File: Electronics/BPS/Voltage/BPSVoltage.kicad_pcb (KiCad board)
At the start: 2 copper layers, 69.9 x 59.7 mm, 72 parts, among them J1 Conn1, J2 Conn2, J3 Conn_01x06, J4 Conn_01x07, Q1 BSS308PE, Q10 BSS308PE, Q11 BSS308PE, Q12 BSS308PE, Q13 BSS308PE, Q2 BSS308PE, Q3 BSS308PE, Q4 BSS308PE, Q5 NSV1C201MZ4, Q6 BSS308PE, Q7 BSS308PE, Q8 BSS308PE, Q9 BSS308PE, U1 LTC6811-1, U2 HX1188FNL

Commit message: Got bored and restructured somewhat.
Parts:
- moved R3 29.4 mm to (176.4, 25.9), turned to 0 degrees
- moved R17 21.8 mm to (211.3, 41.2), turned to 270 degrees
- moved R1 21.8 mm to (181.9, 25.9), turned to 180 degrees
- moved R16 21.0 mm to (209.3, 41.2), turned to 270 degrees
- moved C1 19.7 mm to (188.0, 25.9), turned to 0 degrees
- moved C14 18.5 mm to (199.1, 70.0), turned to 270 degrees
- moved C17 18.4 mm to (195.2, 73.7)
- moved U2 16.6 mm to (206.2, 69.1)
- moved Q5 15.4 mm to (205.7, 31.6)
- moved R23 15.0 mm to (214.8, 49.8), turned to 0 degrees
- moved C18 14.1 mm to (217.7, 58.3)
- moved C10 14.1 mm to (211.3, 35.6), turned to 270 degrees
- moved C15 12.7 mm to (215.9, 44.1), turned to 90 degrees
- moved R24 11.4 mm to (215.8, 60.5)
- moved J1 10.2 mm to (222.9, 52.1)
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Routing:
- net Net-(C3-Pad1): track 7.51 -> 35.0 mm
- net /Batt12: track 49.1 -> 22.7 mm
- net GND: track 29.9 -> 14.6 mm
- net Net-(Q5-Pad1): track 6.05 -> 20.0 mm, vias 0 -> 2
- net Net-(R16-Pad1): track 21.4 -> 7.79 mm
- net Net-(J1-Pad1): track 8.34 -> 21.8 mm
- net /VREG: track 13.1 -> 25.4 mm, vias 0 -> 2
- net Net-(R16-Pad2): track 17.0 -> 5.41 mm
- net Net-(J1-Pad2): track 8.15 -> 19.6 mm
- net /IMA: track 35.5 -> 26.0 mm
- net Net-(Q11-Pad1): track 14.1 -> 22.5 mm, vias 2 -> 0
- net Net-(Q12-Pad1): track 21.6 -> 28.8 mm, vias 2 -> 0
- net Net-(C1-Pad1): track 23.7 -> 30.7 mm
- net Net-(J2-Pad1): track 8.36 -> 15.1 mm
- net Net-(J2-Pad2): track 8.55 -> 14.9 mm
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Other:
- board size 69.9 x 59.7 mm -> 58.4 x 59.7 mm
- board text added: "Chase Block"
- board text added: "UT SVT -- BeVolt"
- board text added: "Voltage Slave 2019"
- board text removed: "2019"
- board text removed: "UT Solar Vehicle Team -- BeVolt"
- board text removed: "Voltage Slave Board Designed by Chase Block"

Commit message: Finished up revision 2 of the board.
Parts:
- added D1: LED, LED_SMD:LED_0805_2012Metric, F.Cu at (134.6, 157.0)
- added D10: LED, LED_SMD:LED_0805_2012Metric, F.Cu at (100.8, 124.2)
- added D11: LED, LED_SMD:LED_0805_2012Metric, F.Cu at (97.8, 124.2)
- added D12: LED, LED_SMD:LED_0805_2012Metric, F.Cu at (94.8, 124.2)
- added D13: LED, LED_SMD:LED_0805_2012Metric, F.Cu at (91.9, 124.2)
- added D2: LED, LED_SMD:LED_0805_2012Metric, F.Cu at (129.8, 124.2)
- added D3: LED, LED_SMD:LED_0805_2012Metric, F.Cu at (126.8, 124.2)
- added D4: LED, LED_SMD:LED_0805_2012Metric, F.Cu at (123.8, 124.2)
- added D5: LED, LED_SMD:LED_0805_2012Metric, F.Cu at (120.8, 124.2)
- added D6: LED, LED_SMD:LED_0805_2012Metric, F.Cu at (117.8, 124.2)
- added D7: LED, LED_SMD:LED_0805_2012Metric, F.Cu at (109.8, 124.2)
- added D8: LED, LED_SMD:LED_0805_2012Metric, F.Cu at (106.8, 124.2)
- added D9: LED, LED_SMD:LED_0805_2012Metric, F.Cu at (103.8, 124.2)
- added J5: Conn_01x03, Connector_PinHeader_2.54mm:PinHeader_1x03_P2.54mm_Vertical, F.Cu at (108.9, 181.5)
- added J6: Conn_01x05, Connector_PinHeader_2.54mm:PinHeader_1x05_P2.54mm_Vertical, F.Cu at (98.9, 181.5)
- added J7: Conn_02x03_Counter_Clockwise, Connector_PinHeader_2.54mm:PinHeader_2x03_P2.54mm_Vertical, F.Cu at (82.5, 168.8)
- added L1: Ferrite_Bead, Inductor_SMD:L_0805_2012Metric, F.Cu at (132.8, 119.3)
- added L10: Ferrite_Bead, Inductor_SMD:L_0805_2012Metric, F.Cu at (100.8, 119.3)
- added L11: Ferrite_Bead, Inductor_SMD:L_0805_2012Metric, F.Cu at (97.8, 119.3)
- added L12: Ferrite_Bead, Inductor_SMD:L_0805_2012Metric, F.Cu at (94.8, 119.3)
- added L13: Ferrite_Bead, Inductor_SMD:L_0805_2012Metric, F.Cu at (91.8, 119.3)
- added L14: Ferrite_Bead, Inductor_SMD:L_0805_2012Metric, F.Cu at (87.3, 119.3)
- added L2: Ferrite_Bead, Inductor_SMD:L_0805_2012Metric, F.Cu at (129.8, 119.3)
- added L3: Ferrite_Bead, Inductor_SMD:L_0805_2012Metric, F.Cu at (126.8, 119.3)
- added L4: Ferrite_Bead, Inductor_SMD:L_0805_2012Metric, F.Cu at (123.8, 119.3)
- added L5: Ferrite_Bead, Inductor_SMD:L_0805_2012Metric, F.Cu at (120.8, 119.3)
- added L6: Ferrite_Bead, Inductor_SMD:L_0805_2012Metric, F.Cu at (117.8, 119.3)
- added L7: Ferrite_Bead, Inductor_SMD:L_0805_2012Metric, F.Cu at (109.8, 119.3)
- added L8: Ferrite_Bead, Inductor_SMD:L_0805_2012Metric, F.Cu at (106.8, 119.3)
- added L9: Ferrite_Bead, Inductor_SMD:L_0805_2012Metric, F.Cu at (103.8, 119.3)
- added MH1: MountingHole, MountingHole:MountingHole_3mm, F.Cu at (141.8, 181.8)
- added MH2: MountingHole, MountingHole:MountingHole_3mm, F.Cu at (141.8, 113.2)
- added MH3: MountingHole, MountingHole:MountingHole_3mm, F.Cu at (83.2, 113.2)
- added MH4: MountingHole, MountingHole:MountingHole_3mm, F.Cu at (83.2, 181.8)
- added R33: 1.5k, Resistor_SMD:R_0805_2012Metric, F.Cu at (134.6, 160.9)
- added R34: 1.2k, Resistor_SMD:R_0805_2012Metric, F.Cu at (129.8, 128.1)
- added R35: 1.2k, Resistor_SMD:R_0805_2012Metric, F.Cu at (126.8, 128.1)
- added R36: 1.2k, Resistor_SMD:R_0805_2012Metric, F.Cu at (123.8, 128.1)
- added R37: 1.2k, Resistor_SMD:R_0805_2012Metric, F.Cu at (120.8, 128.1)
- added R38: 1.2k, Resistor_SMD:R_0805_2012Metric, F.Cu at (117.8, 128.1)
- added R39: 1.2k, Resistor_SMD:R_0805_2012Metric, F.Cu at (109.8, 128.1)
- added R40: 1.2k, Resistor_SMD:R_0805_2012Metric, F.Cu at (106.8, 128.1)
- added R41: 1.2k, Resistor_SMD:R_0805_2012Metric, F.Cu at (103.8, 128.1)
- added R42: 1.2k, Resistor_SMD:R_0805_2012Metric, F.Cu at (100.8, 128.1)
- added R43: 1.2k, Resistor_SMD:R_0805_2012Metric, F.Cu at (97.8, 128.1)
- added R44: 1.2k, Resistor_SMD:R_0805_2012Metric, F.Cu at (94.8, 128.1)
- added R45: 1.2k, Resistor_SMD:R_0805_2012Metric, F.Cu at (91.9, 128.1)
- added TP1: V+, TestPoint:TestPoint_Keystone_5005-5009_Compact, F.Cu at (142.2, 119.3)
- added TP2: VREG, TestPoint:TestPoint_Keystone_5005-5009_Compact, F.Cu at (142.2, 136.6)
- added TP3: GND, TestPoint:TestPoint_Keystone_5005-5009_Compact, F.Cu at (142.2, 129.1)
- R16: value 1k -> 806
- R17: value 1k -> 1.21k
- moved J1 176.3 mm to (84.1, 160.9), turned to 90 degrees
- moved C15 163.6 mm to (102.4, 162.0), turned to 0 degrees
- moved R20 163.1 mm to (97.6, 161.1), turned to 270 degrees
- moved J2 161.9 mm to (84.1, 148.3), turned to 90 degrees
- moved R23 156.4 mm to (102.4, 158.6), turned to 180 degrees
- moved R16 154.5 mm to (118.3, 166.0), turned to 90 degrees
- moved R17 154.5 mm to (120.3, 166.0), turned to 90 degrees
- moved C18 154.4 mm to (85.6, 138.3), turned to 90 degrees
- moved C9 152.9 mm to (113.9, 166.6), turned to 270 degrees
- moved C8 152.7 mm to (111.8, 166.6), turned to 270 degrees
- moved C10 152.6 mm to (130.3, 164.9)
- moved C1 151.4 mm to (128.0, 164.9), turned to 270 degrees
- moved Q5 148.9 mm to (128.0, 158.6)
- moved R24 148.9 mm to (92.7, 144.3)
- moved R27 144.5 mm to (96.7, 144.3), turned to 180 degrees
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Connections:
- net Net-(Q1-Pad3) renamed /L11
- net Net-(Q10-Pad3) renamed /L3
- net Net-(Q11-Pad3) renamed /L2
- net Net-(Q12-Pad3) renamed /L1
- net Net-(Q13-Pad3) renamed /L0
- net Net-(Q2-Pad3) renamed /L10
- net Net-(Q3-Pad3) renamed /L9
- net Net-(Q4-Pad3) renamed /L8
- net Net-(Q6-Pad3) renamed /L7
- net Net-(Q7-Pad3) renamed /L6
- net Net-(Q8-Pad3) renamed /L5
- net Net-(Q9-Pad3) renamed /L4
- C21 pad 1: GND -> /Batt0
- J3 pad 1: /Batt7 -> Net-(J3-Pad1)
- J3 pad 2: /Batt8 -> Net-(J3-Pad2)
- J3 pad 3: /Batt9 -> Net-(J3-Pad3)
- J3 pad 4: /Batt10 -> Net-(J3-Pad4)
- J3 pad 5: /Batt11 -> Net-(J3-Pad5)
- J3 pad 6: /Batt12 -> /V12
- J4 pad 1: GND -> Net-(J4-Pad1)
- J4 pad 2: /Batt1 -> Net-(J4-Pad2)
- J4 pad 3: /Batt2 -> Net-(J4-Pad3)
- J4 pad 4: /Batt3 -> Net-(J4-Pad4)
- J4 pad 5: /Batt4 -> Net-(J4-Pad5)
- J4 pad 6: /Batt5 -> Net-(J4-Pad6)
- J4 pad 7: /Batt6 -> Net-(J4-Pad7)
- R1 pad 2: /Batt12 -> /V12
- R3 pad 1: /Batt12 -> /V12
- R32 pad 1: GND -> /Batt0
- U1 pad 26: GND -> /Batt0
- U1 pad 27: (no net) -> /GPIO1
- U1 pad 28: (no net) -> /GPIO2
- U1 pad 29: (no net) -> /GPIO3
- U1 pad 32: (no net) -> /GPIO4
- U1 pad 33: (no net) -> /GPIO5
- U1 pad 40: /VREG -> /ISOMD
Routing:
- net /Batt0: track 0.00 -> 57.9 mm, vias 0 -> 4
- net /VREG: track 25.4 -> 75.1 mm, vias 2 -> 0
- net /IMA: track 26.0 -> 63.2 mm
- net /IPB: track 36.6 -> 66.7 mm, vias 0 -> 2
- net /GPIO1: track 0.00 -> 27.8 mm
- net /GPIO2: track 0.00 -> 26.0 mm
- net /IMB: track 39.6 -> 65.4 mm
- net /GPIO3: track 0.00 -> 25.2 mm
- net /GPIO4: track 0.00 -> 25.0 mm
- net /GPIO5: track 0.00 -> 24.2 mm
- net /ISOMD: track 0.00 -> 23.0 mm, vias 0 -> 2
- net Net-(C3-Pad1): track 35.0 -> 57.8 mm
- net /IPA: track 23.6 -> 46.1 mm, vias 0 -> 3
- net Net-(C16-Pad1): track 35.3 -> 15.4 mm
- net Net-(C1-Pad1): track 30.7 -> 49.6 mm
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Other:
- board size 58.4 x 59.7 mm -> 65 x 75 mm
- board text added: "GND"
- board text added: "V+"
- board text added: "VREG"
- board text removed: "Chase Block"
- board text removed: "UT SVT -- BeVolt"
- board text removed: "Voltage Slave 2019"

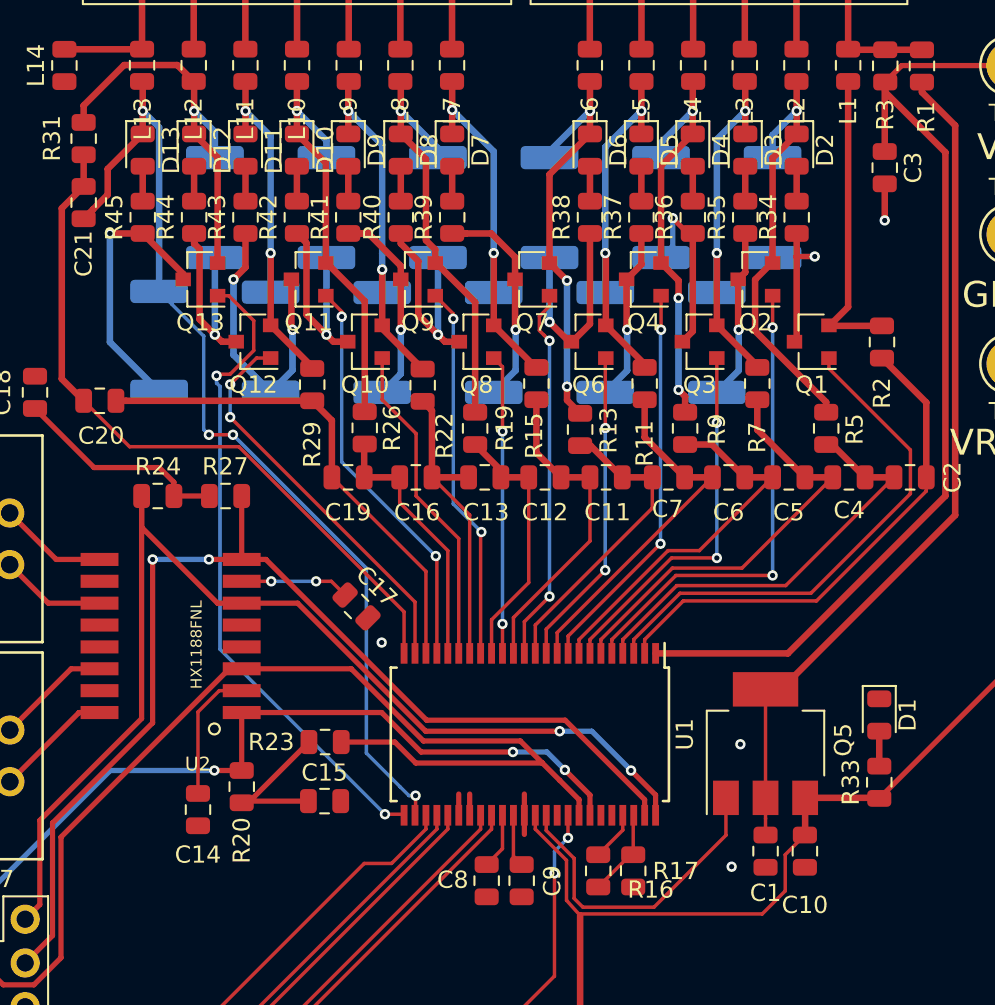
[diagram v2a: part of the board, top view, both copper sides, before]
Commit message: Fixed the via sizes on the voltage board.
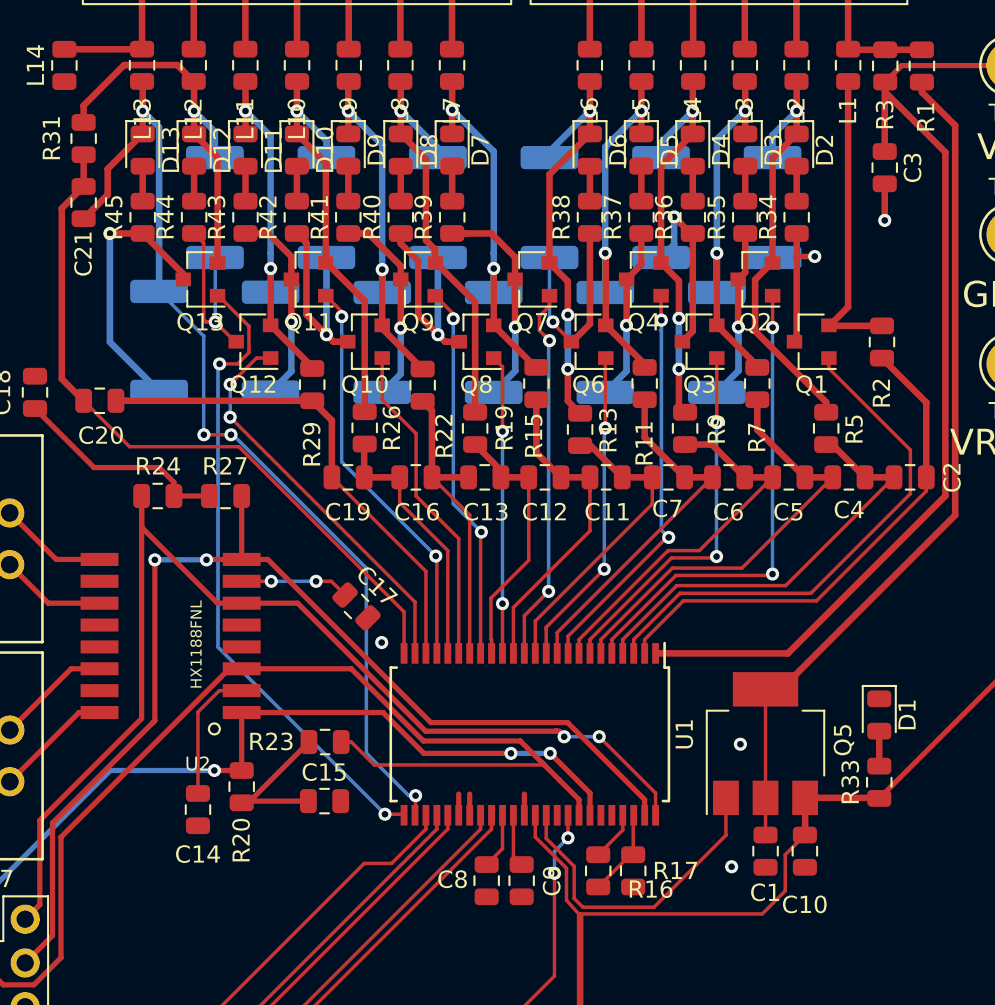
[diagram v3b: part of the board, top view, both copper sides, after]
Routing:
- net /L2: track 17.5 -> 11.6 mm, vias 2 -> 1
- net GND: track 6.94 -> 5.82 mm
- net /Batt6: track 22.3 -> 21.4 mm
- net /Batt2: track 21.9 -> 21.0 mm
- net /L1: track 12.3 -> 11.4 mm
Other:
- net class Default: via_dia 0.8 -> 0.762; via_drill 0.4 -> 0.381
- rule via_min_drill: 0.3 -> 0.381
- rule via_min_size: 0.4 -> 0.762

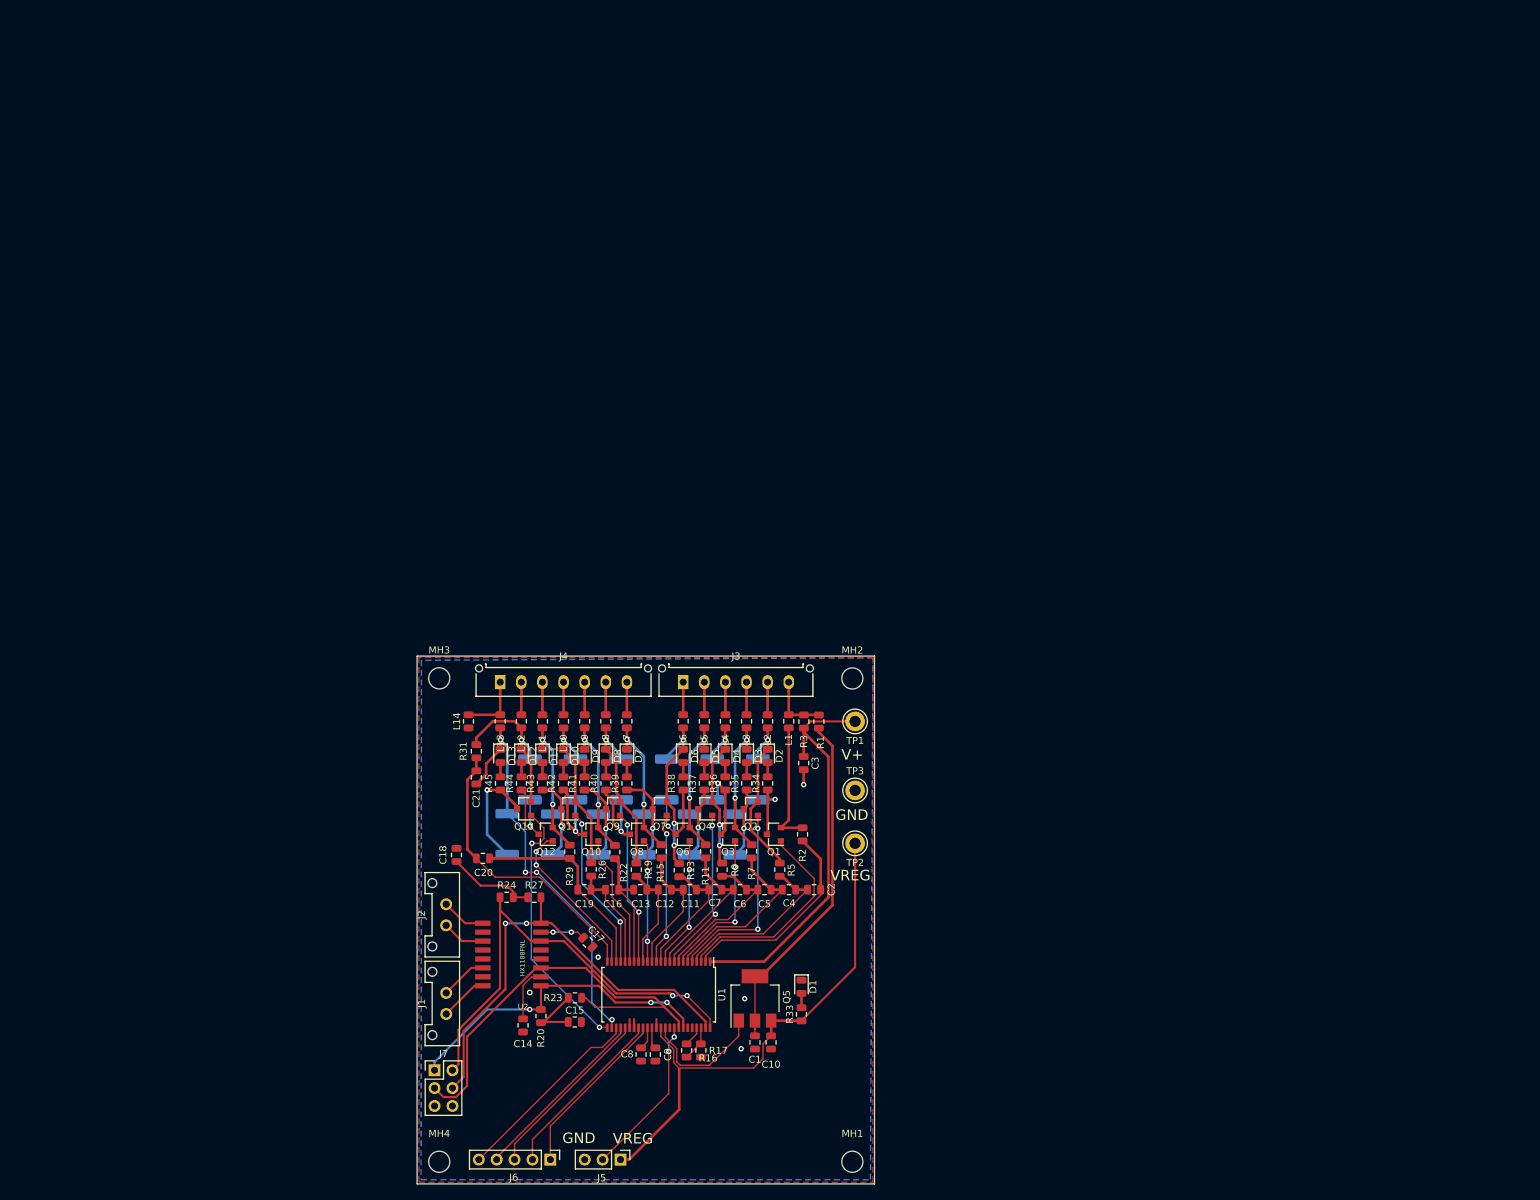
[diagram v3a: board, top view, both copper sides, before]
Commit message: Moved some components around and deleted dimension
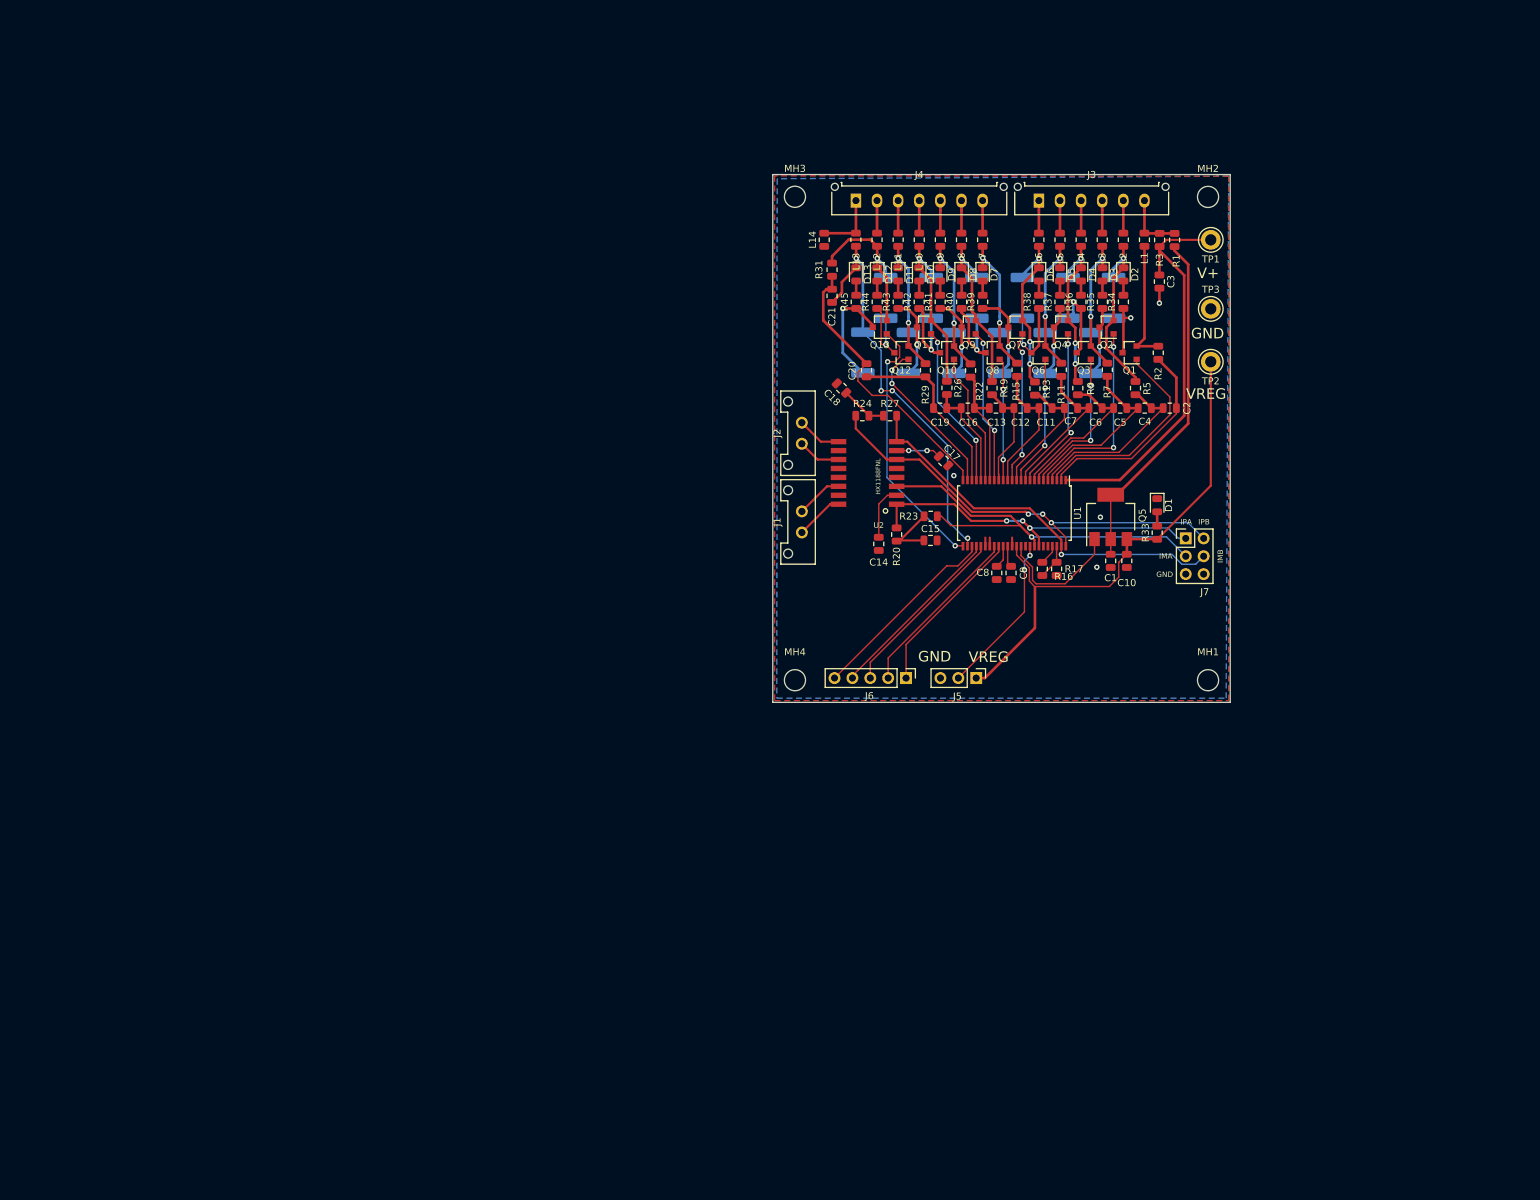
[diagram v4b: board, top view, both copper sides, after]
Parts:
- moved J7 130.8 mm to (189.2, 93.3)
- moved C20 88.2 mm to (143.9, 69.4), turned to 270 degrees
- moved C18 86.0 mm to (140.3, 71.9), turned to 135 degrees
- moved D2 85.1 mm to (180.4, 55.8)
- moved D6 85.1 mm to (168.4, 55.8)
- moved R1 85.1 mm to (187.6, 50.9)
- moved R34 85.1 mm to (180.4, 59.7)
- moved R38 85.1 mm to (168.4, 59.7)
- moved C1 85.1 mm to (178.6, 96.5)
- moved C10 85.1 mm to (180.8, 96.5)
- moved C11 85.1 mm to (169.3, 74.8)
- moved C12 85.1 mm to (165.7, 74.8)
- moved C14 85.1 mm to (145.6, 94.1)
- moved C16 85.1 mm to (158.3, 74.8)
- moved C21 85.1 mm to (139.0, 58.8)
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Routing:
- net /IMB: track 65.3 -> 56.2 mm, vias 2 -> 1
- net Net-(C18-Pad1): track 12.7 -> 6.68 mm
- net /IPB: track 67.1 -> 62.2 mm, vias 2 -> 3
- net /IMA: track 63.3 -> 59.0 mm, vias 0 -> 1
- net /IPA: track 46.2 -> 49.6 mm
- net Net-(C19-Pad1): track 28.8 -> 25.8 mm
- net Net-(C20-Pad1): track 41.4 -> 40.5 mm
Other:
- board text added: "IMA"
- board text added: "IMB"
- board text added: "IPA"
- board text added: "IPB"
